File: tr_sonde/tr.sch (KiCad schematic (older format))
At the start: 84 parts, among them J1 SMA, J2 SMA, J3 SMA, K1 TR, K2 HV_MON, K3 VINHDR, Q1 PBSS4250X, Q2 MMBT2222A, Q3 STD2NK90ZT4, Q4 STD2NK90ZT4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

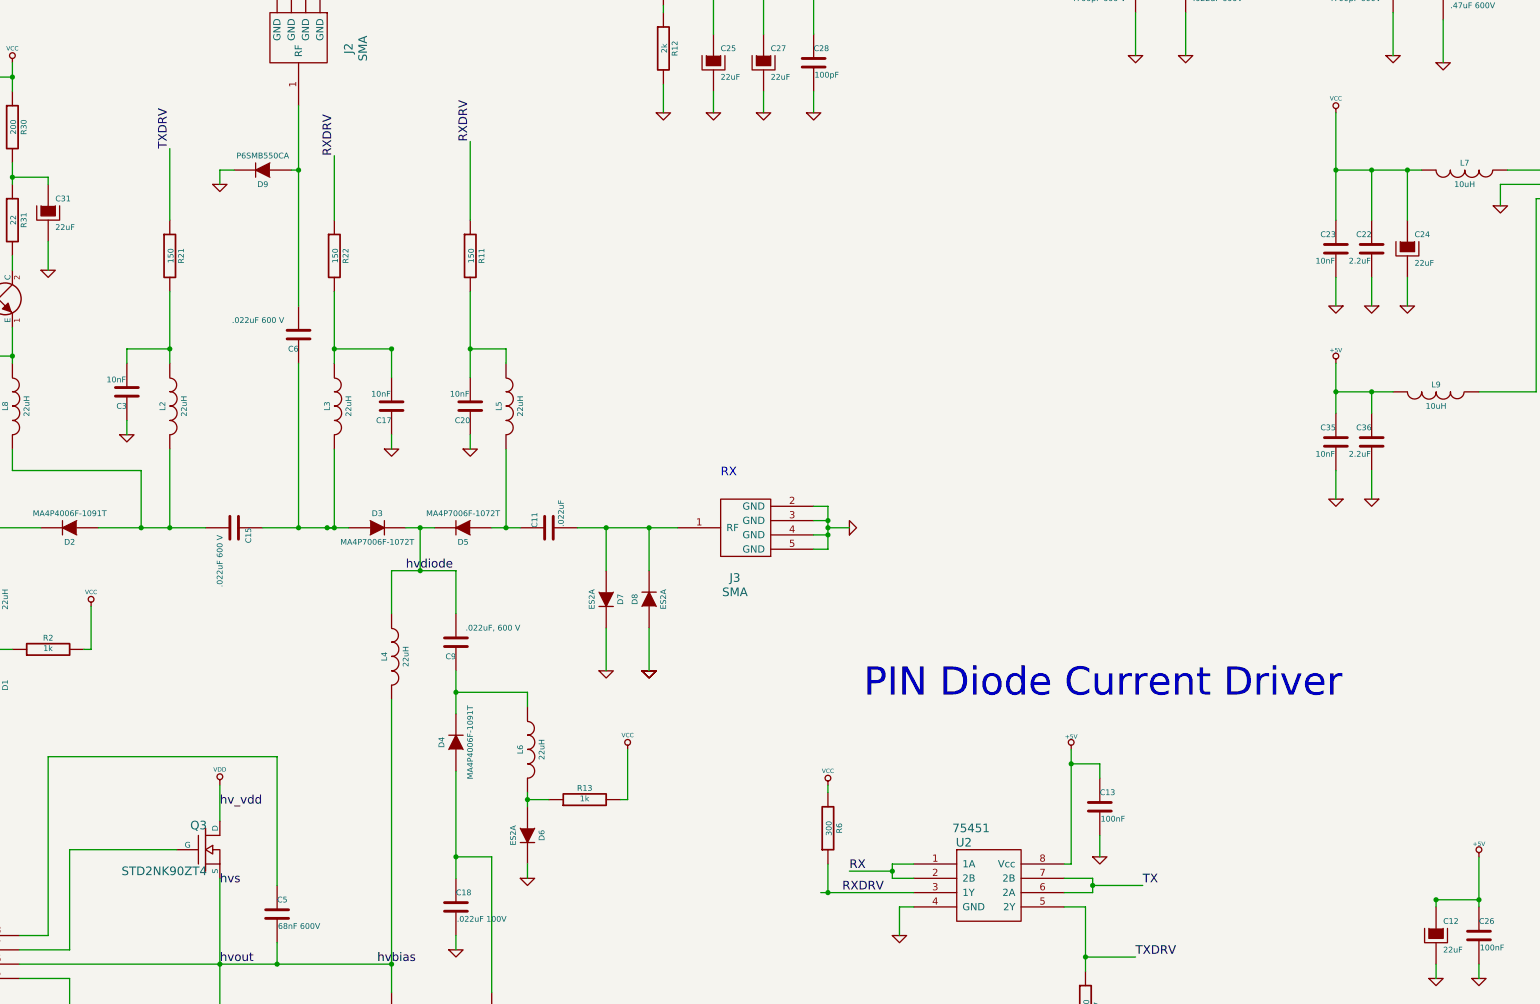
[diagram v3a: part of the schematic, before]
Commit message: moved agc coupled signal splitting off-board
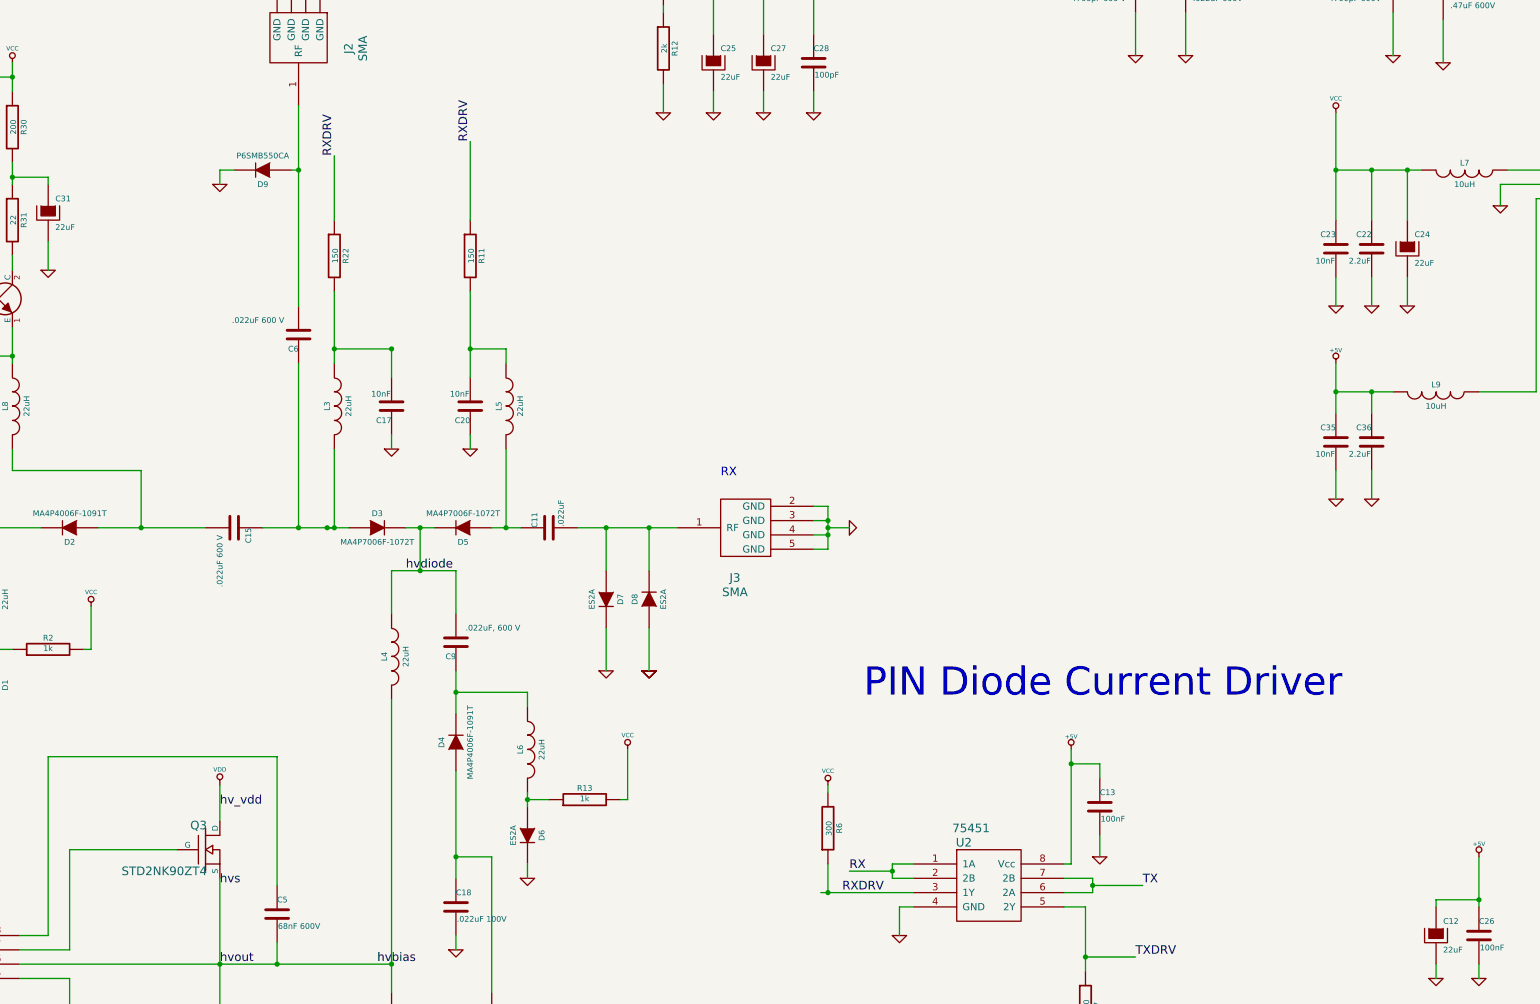
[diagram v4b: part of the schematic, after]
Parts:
- removed C3: 10nF, smd_capacitors:c_0805, symbol C
- removed L2: 22uH, smd_capacitors:c_1210, symbol INDUCTOR
- removed R21: 150, smd_capacitors:c_0805, symbol R
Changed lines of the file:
@@
-$EndComp
-$Comp
-L INDUCTOR L2
-U 1 1 52AA151D
-P 4600 4950
-F 0 "L2" V 4550 4950 40  0000 C CNN
-F 1 "22uH" V 4700 4950 40  0000 C CNN
-F 2 "smd_capacitors:c_1210" H 4600 4950 60  0001 C CNN
-F 3 "~" H 4600 4950 60  0000 C CNN
-	1    4600 4950
-	1    0    0    -1
 $EndComp
 $Comp
@@
 	1    6950 4950
 	1    0    0    -1
-$EndComp
-$Comp
-L C C3
-U 1 1 52AA19DC
-P 4300 4850
-F 0 "C3" H 4300 4950 40  0000 L CNN
-F 1 "10nF" H 4306 4765 40  0000 L CNN
-F 2 "smd_capacitors:c_0805" H 4338 4700 30  0001 C CNN
-F 3 "~" H 4300 4850 60  0000 C CNN
-	1    4300 4850
-	-1   0    0    1
 $EndComp
 $Comp
@@
 $EndComp
 $Comp
-L GND #PWR010
-U 1 1 52AA19EF
-P 4300 5150
-F 0 "#PWR010" H 4300 5150 30  0001 C CNN
-F 1 "GND" H 4300 5080 30  0001 C CNN
-F 2 "" H 4300 5150 60  0000 C CNN
-F 3 "" H 4300 5150 60  0000 C CNN
-	1    4300 5150
-	1    0    0    -1
-$EndComp
-$Comp
 L DIODE D7
 U 1 1 52AA1B5A
@@
 F 3 "" H 6150 5250 60  0000 C CNN
 	1    6150 5250
-	1    0    0    -1
-$EndComp
-$Comp
-L R R21
-U 1 1 52AE7113
-P 4600 3900
-F 0 "R21" V 4680 3900 40  0000 C CNN
-F 1 "150" V 4607 3901 40  0000 C CNN
-F 2 "smd_capacitors:c_0805" V 4530 3900 30  0001 C CNN
-F 3 "~" H 4600 3900 30  0000 C CNN
-	1    4600 3900
 	1    0    0    -1
 $EndComp
@@
 Text Label 6700 3100 1    60   ~ 0
 RXDRV
-Text Label 4600 3150 1    60   ~ 0
-TXDRV
 Text Label 11400 8300 0    60   ~ 0
 TX
@@
 Wire Wire Line
 	9300 1550 9600 1550
-Connection ~ 13450 8400
 Wire Wire Line
 	13450 8450 13450 8400
@@
 Wire Wire Line
 	6850 9550 6850 10150
-Wire Wire Line
-	4600 3150 4600 3650
 Wire Wire Line
 	6700 3100 6700 3650
@@
 	5250 5800 5850 5800
 Wire Wire Line
-	4600 4150 4600 4650
-Wire Wire Line
 	15400 6450 15900 6450
 Wire Wire Line
@@
 Wire Wire Line
 	3550 8850 6150 8850
-Connection ~ 4600 5800
-Wire Wire Line
-	4600 5800 4600 5250
 Wire Wire Line
 	5350 8850 5350 8700
@@
 Connection ~ 6950 5800
 Wire Wire Line
-	4300 5050 4300 5150
-Wire Wire Line
 	6150 6100 6150 6400
 Wire Wire Line
@@
 Wire Wire Line
 	7950 6500 7950 6800
-Connection ~ 4600 4550
 Wire Wire Line
 	6950 5250 6950 5800
@@
 	2400 4450 2600 4450
 Wire Wire Line
-	4300 4550 4600 4550
-Wire Wire Line
 	13450 8400 13750 8400
 Wire Wire Line
@@
 Wire Wire Line
 	6950 4550 6950 4650
-Wire Wire Line
-	4300 4550 4300 4650
 $EndSCHEMATC

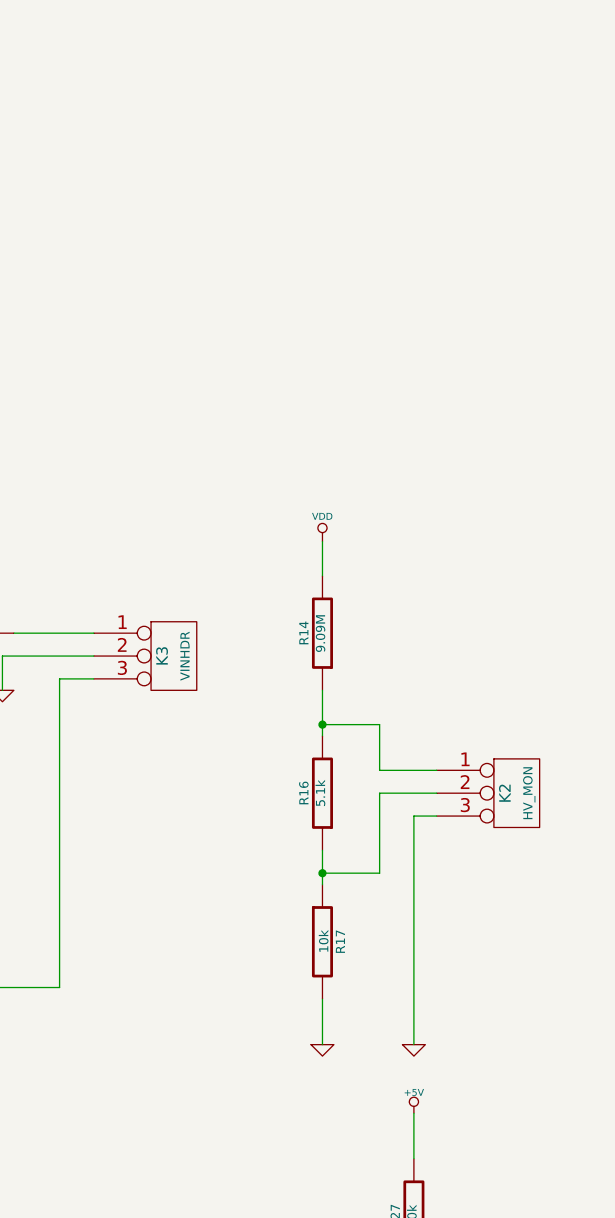
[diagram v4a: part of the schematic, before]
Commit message: added limiters to agc
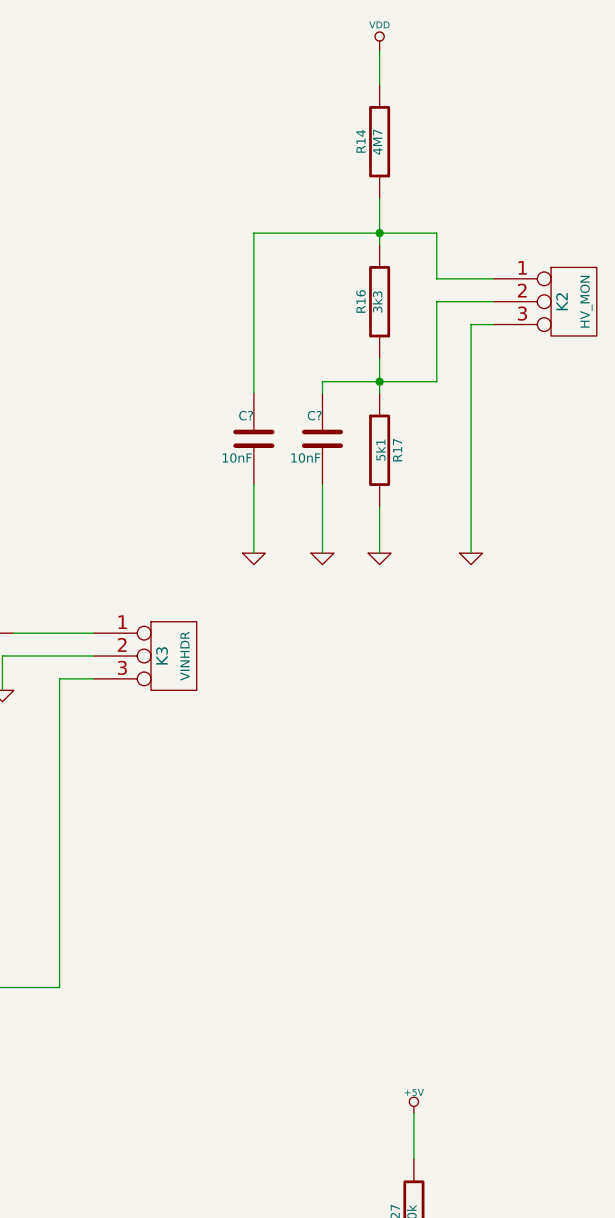
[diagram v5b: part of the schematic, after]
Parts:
- added C? (x2): 10nF, smd_capacitors:c_0805, symbol C
- R14: value 9.09M -> 4M7
- R16: value 5.1k -> 3k3
- R17: value 10k -> 5k1
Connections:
- net GND: now also C?.2, C?.2
- net at K2.1 (P1), R14.1, R16.2: now also C?.1
- net at K2.2 (PM), R16.1, R17.1: now also C?.1
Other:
- moved on the sheet: K2, R14, R16, R17
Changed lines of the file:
@@
 L R R14
 U 1 1 537FA2EB
-P 15300 3300
-F 0 "R14" V 15380 3300 40  0000 C CNN
-F 1 "9.09M" V 15307 3301 40  0000 C CNN
-F 2 "smd_capacitors:c_0805" V 15230 3300 30  0001 C CNN
-F 3 "~" H 15300 3300 30  0000 C CNN
-	1    15300 3300
+P 15550 1150
+F 0 "R14" V 15630 1150 40  0000 C CNN
+F 1 "4M7" V 15557 1151 40  0000 C CNN
+F 2 "smd_capacitors:c_0805" V 15480 1150 30  0001 C CNN
+F 3 "~" H 15550 1150 30  0000 C CNN
+	1    15550 1150
 	-1   0    0    1
 $EndComp
@@
 L R R16
 U 1 1 537FA2F6
-P 15300 4000
-F 0 "R16" V 15380 4000 40  0000 C CNN
-F 1 "5.1k" V 15307 4001 40  0000 C CNN
-F 2 "smd_capacitors:c_0805" V 15230 4000 30  0001 C CNN
-F 3 "~" H 15300 4000 30  0000 C CNN
-	1    15300 4000
+P 15550 1850
+F 0 "R16" V 15630 1850 40  0000 C CNN
+F 1 "3k3" V 15557 1851 40  0000 C CNN
+F 2 "smd_capacitors:c_0805" V 15480 1850 30  0001 C CNN
+F 3 "~" H 15550 1850 30  0000 C CNN
+	1    15550 1850
 	-1   0    0    1
 $EndComp
@@
 L CONN_3 K2
 U 1 1 537FA301
-P 16150 4000
-F 0 "K2" V 16100 4000 50  0000 C CNN
-F 1 "HV_MON" V 16200 4000 40  0000 C CNN
-F 2 "Connect:PINHEAD1-3" H 16150 4000 60  0001 C CNN
-F 3 "~" H 16150 4000 60  0000 C CNN
-	1    16150 4000
+P 16400 1850
+F 0 "K2" V 16350 1850 50  0000 C CNN
+F 1 "HV_MON" V 16450 1850 40  0000 C CNN
+F 2 "Connect:PINHEAD1-3" H 16400 1850 60  0001 C CNN
+F 3 "~" H 16400 1850 60  0000 C CNN
+	1    16400 1850
 	1    0    0    -1
 $EndComp
@@
 L VDD #PWR048
 U 1 1 537FA30C
-P 15300 2900
-F 0 "#PWR048" H 15300 3000 30  0001 C CNN
-F 1 "VDD" H 15300 3010 30  0000 C CNN
-F 2 "" H 15300 2900 60  0000 C CNN
-F 3 "" H 15300 2900 60  0000 C CNN
-	1    15300 2900
+P 15550 750
+F 0 "#PWR048" H 15550 850 30  0001 C CNN
+F 1 "VDD" H 15550 860 30  0000 C CNN
+F 2 "" H 15550 750 60  0000 C CNN
+F 3 "" H 15550 750 60  0000 C CNN
+	1    15550 750
 	1    0    0    -1
 $EndComp
@@
 L GND #PWR049
 U 1 1 537FA865
-P 15300 5100
-F 0 "#PWR049" H 15300 5100 30  0001 C CNN
-F 1 "GND" H 15300 5030 30  0001 C CNN
-F 2 "" H 15300 5100 60  0000 C CNN
-F 3 "" H 15300 5100 60  0000 C CNN
-	1    15300 5100
+P 15550 2950
+F 0 "#PWR049" H 15550 2950 30  0001 C CNN
+F 1 "GND" H 15550 2880 30  0001 C CNN
+F 2 "" H 15550 2950 60  0000 C CNN
+F 3 "" H 15550 2950 60  0000 C CNN
+	1    15550 2950
 	1    0    0    -1
 $EndComp
@@
 L R R17
 U 1 1 537FAAA4
-P 15300 4650
-F 0 "R17" V 15380 4650 40  0000 C CNN
-F 1 "10k" V 15307 4651 40  0000 C CNN
-F 2 "smd_capacitors:c_0805" V 15230 4650 30  0001 C CNN
-F 3 "~" H 15300 4650 30  0000 C CNN
-	1    15300 4650
+P 15550 2500
+F 0 "R17" V 15630 2500 40  0000 C CNN
+F 1 "5k1" V 15557 2501 40  0000 C CNN
+F 2 "smd_capacitors:c_0805" V 15480 2500 30  0001 C CNN
+F 3 "~" H 15550 2500 30  0000 C CNN
+	1    15550 2500
 	1    0    0    -1
 $EndComp
@@
 L GND #PWR050
 U 1 1 537FAD00
-P 15700 5100
-F 0 "#PWR050" H 15700 5100 30  0001 C CNN
-F 1 "GND" H 15700 5030 30  0001 C CNN
-F 2 "" H 15700 5100 60  0000 C CNN
-F 3 "" H 15700 5100 60  0000 C CNN
-	1    15700 5100
+P 15950 2950
+F 0 "#PWR050" H 15950 2950 30  0001 C CNN
+F 1 "GND" H 15950 2880 30  0001 C CNN
+F 2 "" H 15950 2950 60  0000 C CNN
+F 3 "" H 15950 2950 60  0000 C CNN
+	1    15950 2950
 	1    0    0    -1
 $EndComp
@@
 	8050 1400 8050 1750
 Wire Wire Line
-	15700 4100 15700 5100
-Wire Wire Line
-	15800 4100 15700 4100
-Wire Wire Line
-	15300 4900 15300 5100
-Connection ~ 15300 4350
-Wire Wire Line
-	15550 4000 15800 4000
-Wire Wire Line
-	15550 4350 15550 4000
-Wire Wire Line
-	15300 4350 15550 4350
-Wire Wire Line
-	15300 4250 15300 4400
-Connection ~ 15300 3700
-Wire Wire Line
-	15550 3900 15800 3900
-Wire Wire Line
-	15550 3700 15550 3900
-Wire Wire Line
-	15300 3700 15550 3700
-Wire Wire Line
-	15300 3550 15300 3750
-Wire Wire Line
-	15300 2900 15300 3050
+	15950 1950 15950 2950
+Wire Wire Line
+	16050 1950 15950 1950
+Wire Wire Line
+	15550 2750 15550 2950
+Connection ~ 15550 2200
+Wire Wire Line
+	15800 1850 16050 1850
+Wire Wire Line
+	15800 2200 15800 1850
+Wire Wire Line
+	15300 2200 15800 2200
+Wire Wire Line
+	15550 2100 15550 2250
+Connection ~ 15550 1550
+Wire Wire Line
+	15800 1750 16050 1750
+Wire Wire Line
+	15800 1550 15800 1750
+Wire Wire Line
+	15000 1550 15800 1550
+Wire Wire Line
+	15550 1400 15550 1600
+Wire Wire Line
+	15550 750  15550 900
 Wire Wire Line
 	9200 7600 9200 7650
@@
 Wire Wire Line
 	6950 4550 6950 4650
+$Comp
+L C C?
+U 1 1 53D17704
+P 15300 2450
+F 0 "C?" H 15300 2550 40  0000 L CNN
+F 1 "10nF" H 15306 2365 40  0000 L CNN
+F 2 "smd_capacitors:c_0805" H 15338 2300 30  0001 C CNN
+F 3 "~" H 15300 2450 60  0000 C CNN
+	1    15300 2450
+	-1   0    0    -1
+$EndComp
+$Comp
+L C C?
+U 1 1 53D1770F
+P 15000 2450
+F 0 "C?" H 15000 2550 40  0000 L CNN
+F 1 "10nF" H 15006 2365 40  0000 L CNN
+F 2 "smd_capacitors:c_0805" H 15038 2300 30  0001 C CNN
+F 3 "~" H 15000 2450 60  0000 C CNN
+	1    15000 2450
+	-1   0    0    -1
+$EndComp
+$Comp
+L GND #PWR?
+U 1 1 53D1771A
+P 15300 2950
+F 0 "#PWR?" H 15300 2950 30  0001 C CNN
+F 1 "GND" H 15300 2880 30  0001 C CNN
+F 2 "" H 15300 2950 60  0000 C CNN
+F 3 "" H 15300 2950 60  0000 C CNN
+	1    15300 2950
+	1    0    0    -1
+$EndComp
+$Comp
+L GND #PWR?
+U 1 1 53D17725
+P 15000 2950
+F 0 "#PWR?" H 15000 2950 30  0001 C CNN
+F 1 "GND" H 15000 2880 30  0001 C CNN
+F 2 "" H 15000 2950 60  0000 C CNN
+F 3 "" H 15000 2950 60  0000 C CNN
+	1    15000 2950
+	1    0    0    -1
+$EndComp
+Wire Wire Line
+	15000 2650 15000 2950
+Wire Wire Line
+	15300 2650 15300 2950
+Wire Wire Line
+	15300 2200 15300 2250
+Wire Wire Line
+	15000 1550 15000 2250
 $EndSCHEMATC
